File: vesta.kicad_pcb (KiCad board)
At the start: 4 copper layers, 0 parts

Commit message: feat: adding the components to the PCB
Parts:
- added BATTERY1: WAFER-PH2_0-2PWZ, JLCImport:WAFER-PH2_0-2PWZ, F.Cu at (89.5, 66.8)
- added C1: 10uF, Capacitor_SMD:C_0805_2012Metric, F.Cu at (87.2, 84.9)
- added C10: 100nF, PCM_JLCPCB:C_0603, F.Cu at (91.4, 76.1)
- added C11: 100nF, PCM_JLCPCB:C_0603, F.Cu at (91.4, 78.3)
- added C12: 100nF, PCM_JLCPCB:C_0603, F.Cu at (91.4, 80.6)
- added C13: 100nF, PCM_JLCPCB:C_0603, F.Cu at (95.2, 69.3)
- added C14: 4.7uF, PCM_JLCPCB:C_0805, F.Cu at (87.2, 81.9)
- added C15: 100nF, PCM_JLCPCB:C_0603, F.Cu at (95.2, 71.6)
- added C16: 100pF, PCM_JLCPCB:C_0402, F.Cu at (98.6, 80.4)
- added C17: 100pF, PCM_JLCPCB:C_0402, F.Cu at (98.6, 82.2)
- added C18: 100pF, PCM_JLCPCB:C_0402, F.Cu at (98.6, 84.1)
- added C19: 100nF, PCM_JLCPCB:C_0603, F.Cu at (95.2, 73.8)
- added C2: 100nF, Capacitor_SMD:C_0603_1608Metric, F.Cu at (102.0, 85.7)
- added C20: DNP, Capacitor_SMD:C_0603_1608Metric, F.Cu at (102.0, 88.2)
- added C21: DNP, Capacitor_SMD:C_0603_1608Metric, F.Cu at (102.0, 90.8)
- added C22: 100nF, PCM_JLCPCB:C_0603, F.Cu at (95.2, 76.1)
- added C23: 100nF, PCM_JLCPCB:C_0603, F.Cu at (95.2, 78.3)
- added C3: 10uF, PCM_JLCPCB:C_0805, F.Cu at (87.2, 69.7)
- added C4: 10uF, PCM_JLCPCB:C_0805, F.Cu at (87.2, 72.8)
- added C5: 10uF, PCM_JLCPCB:C_0805, F.Cu at (87.2, 75.8)
- added C6: 22uF, PCM_JLCPCB:C_0805, F.Cu at (87.2, 78.9)
- added C7: 470nF, PCM_JLCPCB:C_0603, F.Cu at (91.4, 69.3)
- added C8: 1uF, PCM_JLCPCB:C_0603, F.Cu at (91.4, 71.6)
- added C9: 10nF, PCM_JLCPCB:C_0603, F.Cu at (91.4, 73.8)
- added D1: D_TVS, Diode_SMD:D_SOD-123, F.Cu at (111.0, 87.3)
- added FL1: BALFHB-WL-05D3, JLCImport:BALFHB-WL-05D3, F.Cu at (105.9, 90.2)
- added J1: Solar Panel, JLCImport:WAFER-PH2_0-2PWZ, F.Cu at (95.9, 66.9)
- added J2: Solar Panel, JLCImport:WAFER-PH2_0-2PWZ, F.Cu at (103.1, 66.9)
- added J3: Conn_ARM_SWD_TagConnect_TC2030-NL, Connector:Tag-Connect_TC2030-IDC-NL_2x03_P1.27mm_Vertical, F.Cu at (104.0, 82.0)
- added J4: U.FL, PCM_JLCPCB:IPEX-SMD_BWIPX-1-001E, F.Cu at (113.8, 62.5)
- added JP_TMR_DISABLE1: SolderJumper_2_Open, Jumper:SolderJumper-2_P1.3mm_Open_RoundedPad1.0x1.5mm, F.Cu at (87.2, 88.2)
- added J_EXP1: Conn_01x10, Connector_PinHeader_1.00mm:PinHeader_1x10_P1.00mm_Horizontal, F.Cu at (91.0, 83.2)
- added L1: FTC252012S2R2MBCA, JLCImport:FTC252012S2R2MBCA, F.Cu at (115.7, 87.2)
- added L3: FNR5040S150MT, JLCImport:FNR5040S150MT, F.Cu at (111.6, 82.5)
- added R1: 8.0kΩ, PCM_JLCPCB:R_0603, F.Cu at (99.0, 69.3)
- added R10: 36.5kΩ, PCM_JLCPCB:R_0603, F.Cu at (102.6, 78.3)
- added R11: 100kΩ, PCM_JLCPCB:R_0402, F.Cu at (98.6, 85.9)
- added R12: 100kΩ, PCM_JLCPCB:R_0603, F.Cu at (106.3, 69.3)
- added R13: 0Ω, PCM_JLCPCB:R_0402, F.Cu at (98.6, 87.8)
- added R14: 0kΩ, PCM_JLCPCB:R_0603, F.Cu at (106.3, 71.6)
- added R15: 10kΩ, PCM_JLCPCB:R_0603, F.Cu at (106.3, 73.8)
- added R16: 10kΩ, PCM_JLCPCB:R_0603, F.Cu at (106.3, 76.1)
- added R2: 8.87(or 8.9)kΩ, PCM_JLCPCB:R_0603, F.Cu at (99.0, 71.6)
- added R3: 10kΩ, PCM_JLCPCB:R_0603, F.Cu at (99.0, 73.8)
- added R4: 100kΩ, PCM_JLCPCB:R_0603, F.Cu at (99.0, 76.1)
- added R5: 100kΩ, PCM_JLCPCB:R_0603, F.Cu at (99.0, 78.3)
- added R6: 100kΩ, PCM_JLCPCB:R_0603, F.Cu at (102.6, 69.3)
- added R7: 72kΩ, PCM_JLCPCB:R_0603, F.Cu at (102.6, 71.6)
- added R8: 16.2kΩ, PCM_JLCPCB:R_0603, F.Cu at (102.6, 73.8)
- added R9: 0kΩ, PCM_JLCPCB:R_0603, F.Cu at (102.6, 76.1)
- added TP1: TP_SYS_RAW, TestPoint:TestPoint_Pad_D1.5mm, F.Cu at (115.5, 90.8)
- added TP2: TP_3V3_SYS, TestPoint:TestPoint_Pad_D1.0mm, F.Cu at (116.7, 81.0)
- added TP3: TP_BOOT0, TestPoint:TestPoint_Pad_D1.0mm, F.Cu at (116.7, 84.0)
- added U1: STM32WL55CCU6, JLCImport:STM32WL55CCU6, F.Cu at (112.6, 72.7)
- added U2: BQ24074RGTR, Package_DFN_QFN:MPS_QFN-16_3x3mm_P0.5mm, F.Cu at (111.1, 91.6)
- added U3: TPS63900DSKR, JLCImport:TPS63900DSKR, F.Cu at (109.2, 66.2)
- added U4: BME688_C3664478, JLCImport:BME688_C3664478, F.Cu at (109.1, 62.2)
- added U6: PE4259-63, JLCImport:PE4259-63, F.Cu at (106.1, 86.2)
- added X1: Q13FC1350000400, PCM_JLCPCB:FC-135R_L3.2-W1.5, F.Cu at (114.3, 66.5)
- added X2: X201632MMB4SI, JLCImport:X201632MMB4SI, F.Cu at (87.2, 91.7)

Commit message: feat: making the pinecone
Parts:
- J3: value Conn_ARM_SWD_TagConnect_TC2030-NL -> TagConnect
- moved C21 87.9 mm to (29.5, 41.0), turned to 180 degrees
- moved L1 87.8 mm to (34.2, 54.7), turned to 180 degrees
- moved U6 87.6 mm to (28.1, 46.4)
- moved FL1 85.8 mm to (32.1, 46.4), turned to 180 degrees
- moved C20 85.7 mm to (29.5, 42.5), turned to 180 degrees
- moved TP3 85.6 mm to (48.2, 32.5), turned to 90 degrees
- moved J4 85.1 mm to (39.5, 21.0)
- moved X1 82.1 mm to (40.2, 31.0), turned to 180 degrees
- moved U1 81.6 mm to (39.0, 37.5), turned to 90 degrees
- moved R13 80.5 mm to (32.0, 42.5), turned to 180 degrees
- moved C18 79.4 mm to (30.0, 44.0), turned to 180 degrees
- moved X2 79.3 mm to (36.2, 31.0), turned to 90 degrees
- moved R12 78.2 mm to (32.5, 43.5)
- moved U2 78.0 mm to (40.0, 59.5)
- moved C17 77.5 mm to (30.1, 45.9), turned to -90 degrees
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- renumbered JP_TMR_DISABLE1 to JP_TMR
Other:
- board outline added: 43 x 61.1 mm
- board text added: "()()() ()()()()() ()()()()()() ()()()()()()() ()()()()()()()() ()()()()()()()()() ()()()()()()()()()() ()()()()()()()()()()() ()()()()()()()()()()()() ()()()()()()()()()()() ()()()()()()()()()() ()()()()()()()() ()()()()()"
- board text added: "()()() ()()()()() ()()()()()()() ()()()()()()()() ()()()()()()()()()()() ()()()()()()()()()()() ()()()()()()()()()()()() ()()()()()()()()()()()()() ()()()()()()()()()()()()()() ()()()()()()()()()()()()()()() ()()()()()()()()()()()()()()()() ()()()()()()()()()()()()()()()()() ()()()()()()()()()()()()()()()()() ()()()()()()()()()()()()()()()()() ()()()()()()()()()()()()()()()()() ()()()()()()()()()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"

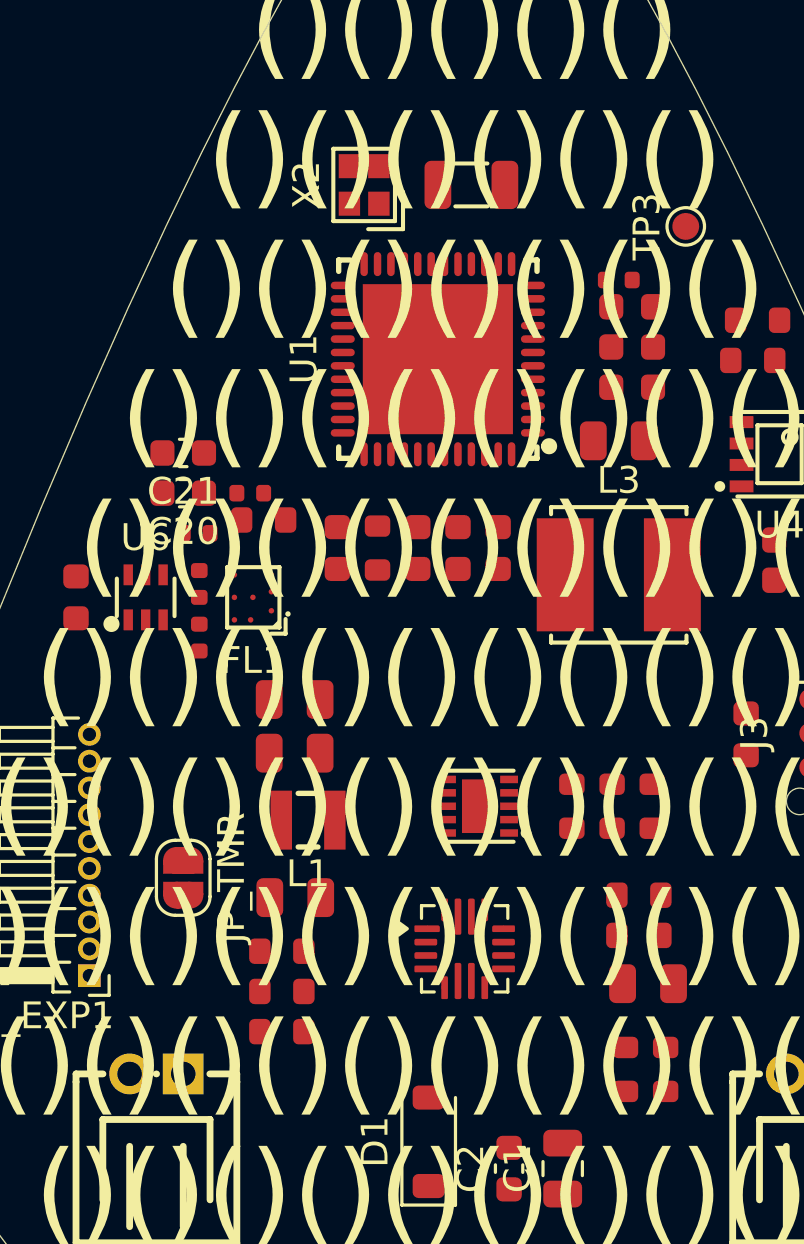
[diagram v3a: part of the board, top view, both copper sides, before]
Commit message: feat: updating the pins in the stm32 footprint
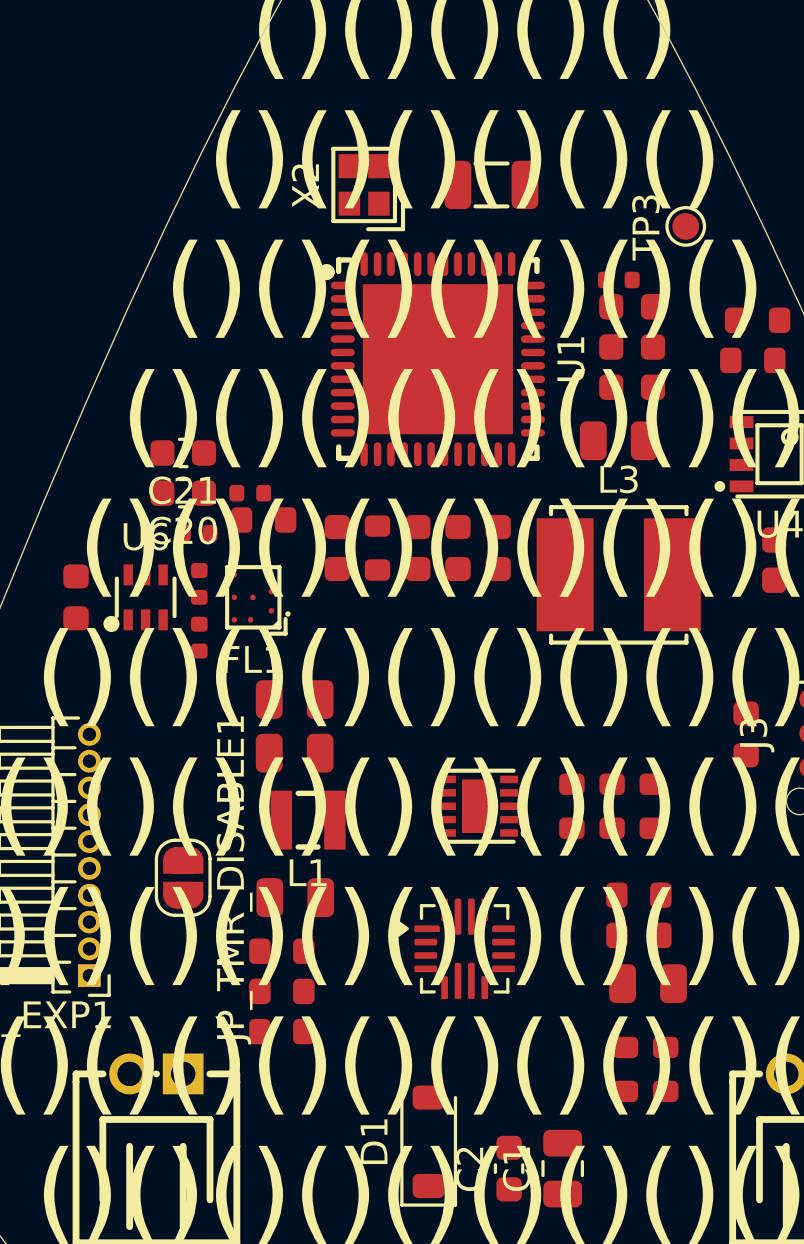
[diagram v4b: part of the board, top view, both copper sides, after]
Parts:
- J3: value TagConnect -> Conn_ARM_SWD_TagConnect_TC2030-NL
- moved X1 0.75 mm to (41.0, 31.0)
- turned U1 to -90 degrees
- renumbered JP_TMR to JP_TMR_DISABLE1
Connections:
- L3 pad 1: unconnected-(L3-Pad1) -> Net-(U1-VLXSMPS)
- U1 pad 1: unconnected-(U1-PB3-Pad1) -> /SWO
- U1 pad 24: unconnected-(U1-VR_PA-Pad24) -> /VR_PA_RF
- U1 pad 25: unconnected-(U1-VDDPA-Pad25) -> /SMPS_1V55
- U1 pad 26: unconnected-(U1-OSC_IN-Pad26) -> /OSC_IN
- U1 pad 47: unconnected-(U1-VLXSMPS-Pad47) -> Net-(U1-VLXSMPS)
- U1 pad 48: unconnected-(U1-VSSSMPS-Pad48) -> GND

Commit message: feat: created the nets
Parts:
- moved U6 25.5 mm to (43.1, 25.8), turned to 180 degrees
- moved C18 19.0 mm to (35.6, 25.8)
- moved C20 18.9 mm to (39.4, 26.3)
- moved C21 18.9 mm to (39.4, 24.8)
- moved R13 18.0 mm to (35.6, 24.8), turned to 0 degrees
- moved X1 10.1 mm to (31.5, 34.5)
- moved X2 9.38 mm to (30.0, 38.0)
- moved J3 2.67 mm to (55.9, 52.7)
- moved J1 1.00 mm to (27.5, 64.2)
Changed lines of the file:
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@@
 	(layers
 		(0 "F.Cu" signal "Front")
-		(4 "In1.Cu" signal)
-		(6 "In2.Cu" signal)
+		(4 "In1.Cu" signal "GND")
+		(6 "In2.Cu" signal "PWR")
 		(2 "B.Cu" signal "Back")
 		(13 "F.Paste" user)
@@
 		(capping no)
 		(filling no)
+		(zone_defaults)
 		(pcbplotparams
 			(layerselection 0x00000000_00000000_55555555_5755f5ff)
@@
 	(footprint "JLCImport:PE4259-63"
 		(layer "F.Cu")
-		(at 28.099314 46.3873)
+		(at 43.149987 25.83998 180)
 		(descr "-40℃~+85℃ 0.35dB 1.8V~3.3V 10MHz~3GHz 30dB 33.5dBm Integrated control logic SPDT SC-70-6 RF Switches ROHS")
 		(tags "C470892 PE4259-63 SC-70-6_L2.2-W1.3-P0.65-LS2.1-BL pSemi")
@@
 		)
 		(property "Manufacturer" "pSemi"
-			(at 0 0 0)
+			(at 0 0 180)
 			(unlocked yes)
 			(layer "F.Fab")
@@
 		)
 		(property "Manufacturer Part" "PE4259-63"
-			(at 0 0 0)
+			(at 0 0 180)
 			(unlocked yes)
 			(layer "F.Fab")
@@
 		(duplicate_pad_numbers_are_jumpers no)
 		(fp_line
-			(start -1.0762 0.701194)
-			(end -1.0762 -0.701194)
+			(start 1.0762 0.701194)
+			(end 1.0762 -0.701194)
 			(stroke
 				(width 0.1524)
@@
 		)
 		(fp_line
-			(start 1.0762 0.701194)
-			(end 1.0762 -0.701194)
+			(start -1.0762 0.701194)
+			(end -1.0762 -0.701194)
 			(stroke
 				(width 0.1524)
@@
 		)
 		(pad "1" smd rect
-			(at -0.649987 0.83998)
+			(at -0.649987 0.83998 180)
 			(size 0.350013 0.78001)
 			(layers "F.Cu" "F.Mask" "F.Paste")
@@
 		)
 		(pad "2" smd rect
-			(at 0 0.83998)
+			(at 0 0.83998 180)
 			(size 0.350013 0.78001)
 			(layers "F.Cu" "F.Mask" "F.Paste")
@@
 		)
 		(pad "3" smd rect
-			(at 0.649987 0.83998)
+			(at 0.649987 0.83998 180)
 			(size 0.350013 0.78001)
 			(layers "F.Cu" "F.Mask" "F.Paste")
@@
 		)
 		(pad "4" smd rect
-			(at 0.649987 -0.83998)
+			(at 0.649987 -0.83998 180)
 			(size 0.350013 0.78001)
 			(layers "F.Cu" "F.Mask" "F.Paste")
@@
 		)
 		(pad "5" smd rect
-			(at 0 -0.83998)
+			(at 0 -0.83998 180)
 			(size 0.350013 0.78001)
 			(layers "F.Cu" "F.Mask" "F.Paste")
@@
 		)
 		(pad "6" smd rect
-			(at -0.649987 -0.83998)
+			(at -0.649987 -0.83998 180)
 			(size 0.350013 0.78001)
 			(layers "F.Cu" "F.Mask" "F.Paste")
@@
 	(footprint "Capacitor_SMD:C_0603_1608Metric"
 		(layer "F.Cu")
-		(at 29.5 42.5 180)
+		(at 39.374987 26.33998 180)
 		(descr "Capacitor SMD 0603 (1608 Metric), square (rectangular) end terminal, IPC-7351 nominal, (Body size source: IPC-SM-782 page 76, https://www.pcb-3d.com/wordpress/wp-content/uploads/ipc-sm-782a_amendment_1_and_2.pdf)")
 		(tags "capacitor")
@@
 	(footprint "JLCImport:X201632MMB4SI"
 		(layer "F.Cu")
-		(at 36.25 31 90)
+		(at 30 38 90)
 		(descr "-40℃~+85℃ 10pF 32MHz Crystal Oscillator ±10ppm ±20ppm SMD2016-4P Crystals ROHS")
 		(tags "C383840 CRYSTAL-SMD_4P-L2.0-W1.6-BL X201632MMB4SI YXC Crystal Oscillators")
@@
 	(footprint "PCM_JLCPCB:C_0402"
 		(layer "F.Cu")
-		(at 30 44 180)
+		(at 35.649987 25.83998 180)
 		(descr "Capacitor SMD 0402 (1005 Metric), square (rectangular) end terminal, IPC_7351 nominal, (Body size source: IPC-SM-782 page 76, https://www.pcb-3d.com/wordpress/wp-content/uploads/ipc-sm-782a_amendment_1_and_2.pdf), generated with kicad-footprint-generator")
 		(tags "capacitor")
@@
 	(footprint "PCM_JLCPCB:R_0402"
 		(layer "F.Cu")
-		(at 32 42.5 180)
+		(at 35.649987 24.83998)
 		(descr "Resistor SMD 0402 (1005 Metric), square (rectangular) end terminal, IPC_7351 nominal, (Body size source: IPC-SM-782 page 72, https://www.pcb-3d.com/wordpress/wp-content/uploads/ipc-sm-782a_amendment_1_and_2.pdf), generated with kicad-footprint-generator")
 		(tags "resistor")
@@
 					(thickness 0.15)
 				)
-				(justify right)
+				(justify left)
 			)
 		)
@@
 		)
 		(property "Datasheet" ""
-			(at 0 0 180)
+			(at 0 0 0)
 			(unlocked yes)
 			(layer "F.Fab")
@@
 		)
 		(property "Description" "Resistor"
-			(at 0 0 180)
+			(at 0 0 0)
 			(unlocked yes)
 			(layer "F.Fab")
@@
 		(duplicate_pad_numbers_are_jumpers no)
 		(fp_line
-			(start 0.9 0.4)
+			(start -0.9 -0.4)
 			(end -0.9 0.4)
 			(stroke
@@
 		)
 		(fp_line
-			(start 0.9 -0.4)
-			(end 0.9 0.4)
+			(start -0.9 -0.4)
+			(end 0.9 -0.4)
 			(stroke
 				(width 0.05)
@@
 		)
 		(fp_line
-			(start -0.9 -0.4)
-			(end 0.9 -0.4)
+			(start 0.9 -0.4)
+			(end 0.9 0.4)
 			(stroke
 				(width 0.05)
@@
 		)
 		(fp_line
-			(start -0.9 -0.4)
+			(start 0.9 0.4)
 			(end -0.9 0.4)
 			(stroke
@@
 		)
 		(pad "1" smd roundrect
-			(at -0.5 0 180)
+			(at -0.5 0)
 			(size 0.56 0.62)
 			(layers "F.Cu" "F.Mask" "F.Paste")
@@
 		)
 		(pad "2" smd roundrect
-			(at 0.5 0 180)
+			(at 0.5 0)
 			(size 0.56 0.62)
 			(layers "F.Cu" "F.Mask" "F.Paste")
@@
 	(footprint "Capacitor_SMD:C_0603_1608Metric"
 		(layer "F.Cu")
-		(at 29.5 41 180)
+		(at 39.374987 24.83998 180)
 		(descr "Capacitor SMD 0603 (1608 Metric), square (rectangular) end terminal, IPC-7351 nominal, (Body size source: IPC-SM-782 page 76, https://www.pcb-3d.com/wordpress/wp-content/uploads/ipc-sm-782a_amendment_1_and_2.pdf)")
 		(tags "capacitor")
@@
 	(footprint "PCM_JLCPCB:FC-135R_L3.2-W1.5"
 		(layer "F.Cu")
-		(at 41 31 180)
+		(at 31.5 34.5 180)
 		(descr "FC-135R_L3.2-W1.5 footprint")
 		(tags "FC-135R_L3.2-W1.5 footprint C32346")
@@
 	(footprint "Connector:Tag-Connect_TC2030-IDC-NL_2x03_P1.27mm_Vertical"
 		(layer "F.Cu")
-		(at 53.516 51.46 -90)
+		(at 55.865 52.73 -90)
 		(descr "Tag-Connect programming header; http://www.tag-connect.com/Materials/TC2030-IDC-NL.pdf")
 		(tags "tag connect programming header pogo pins")
@@
 			(polygon
 				(pts
-					(xy 54.151 52.73) (xy 54.151 50.19) (xy 52.881 50.19) (xy 52.881 52.73)
+					(xy 56.5 54) (xy 56.5 51.46) (xy 55.23 51.46) (xy 55.23 54)
 				)
 			)
@@
 	(footprint "JLCImport:WAFER-PH2_0-2PWZ"
 		(layer "F.Cu")
-		(at 28.499238 64.167526 180)
+		(at 27.5 64.167526 180)
 		(descr "-25℃~+85℃ 1 1x2P 2 250V 2A 2P 2mm 4.7mm 6.05mm 6mm Brass PA66 PH Right Angle Tin UL94V-0 White 弯插,P=2mm Wire To Board Connector ROHS")
 		(tags "C5359610 CONN-TH_2P-P2.00_GP01-2001WR-2P WAFER-PH2.0-2PWZ XUNPU")
@@
 		)
 	)
+	(segment
+		(start 43.149987 24.58998)
+		(end 43.149987 25)
+		(width 0.4)
+		(layer "F.Cu")
+		(net "GND")
+	)
 	(embedded_fonts no)

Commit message: feat: doing all the critical connections
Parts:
- removed R7: 72kΩ, PCM_JLCPCB:R_0603
- moved C19 24.7 mm to (43.5, 29.5), turned to 180 degrees
- moved C16 22.3 mm to (44.0, 30.5), turned to 0 degrees
- moved C17 20.0 mm to (44.0, 31.5), turned to 0 degrees
- moved R12 19.0 mm to (43.5, 28.0), turned to 180 degrees
- moved FL1 16.1 mm to (37.7, 31.3), turned to 90 degrees
- moved C13 15.8 mm to (30.5, 36.5), turned to 180 degrees
- moved BATTERY1 15.4 mm to (54.0, 64.2)
- moved J2 14.2 mm to (40.5, 71.0)
- moved R2 14.2 mm to (46.5, 64.5), turned to 180 degrees
- moved R4 13.9 mm to (46.5, 58.5), turned to 180 degrees
- moved R6 13.7 mm to (35.7, 57.0), turned to 0 degrees
- moved JP_TMR_DISABLE1 13.7 mm to (41.0, 64.3)
- moved C5 13.5 mm to (46.5, 56.5), turned to 180 degrees
- moved R3 13.5 mm to (46.5, 63.0), turned to 180 degrees
- moved C3 13.1 mm to (46.5, 60.5), turned to 0 degrees
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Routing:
- net /3V3_SYS: track 0.00 -> 61.8 mm, vias 0 -> 5
- net GND: track 0.41 -> 36.9 mm
- net /SWCLK: track 0.00 -> 30.1 mm, vias 0 -> 2
- net /SMPS_1V55: track 0.00 -> 30.0 mm
- net /VIN_SOLAR: track 0.00 -> 28.1 mm
- net /RF_SW_CTRL: track 0.00 -> 25.5 mm, vias 0 -> 2
- net /SYS_RAW: track 0.00 -> 20.6 mm
- net /BAT_RAW: track 0.00 -> 16.1 mm
- net /PH3-BOOT0: track 0.00 -> 9.70 mm
- net Net-(U6-RFC): track 0.00 -> 9.20 mm
- net /PC15-OSC32_OUT: track 0.00 -> 8.99 mm
- net Net-(U6-RF2): track 0.00 -> 8.99 mm
- net Net-(J4-In): track 0.00 -> 8.82 mm
- net Net-(U1-VLXSMPS): track 0.00 -> 8.61 mm
- net /VDDA: track 0.00 -> 7.99 mm
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- added copper zone on In2.Cu, net /3V3_SYS
- added copper zone on In1.Cu, net GND

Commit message: feat: finishing all the connections
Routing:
- net /I2C1_SDA: track 6.00 -> 45.2 mm, vias 0 -> 1
- net /I2C1_SCL: track 2.81 -> 37.7 mm, vias 0 -> 1
- net /SWDIO: track 3.84 -> 38.0 mm
- net /EXP_SPI_CS0: track 0.00 -> 32.5 mm, vias 0 -> 1
- net /SPI1_SCK: track 0.00 -> 31.0 mm, vias 0 -> 1
- net /SPI1_MISO: track 0.00 -> 29.9 mm, vias 0 -> 1
- net /EXP_GPIO_CS1: track 0.00 -> 25.6 mm, vias 0 -> 1
- net /EXP_INT_WAKE: track 0.00 -> 24.7 mm, vias 0 -> 1
- net GND: track 36.9 -> 60.3 mm, vias 0 -> 19
- net /SMPS_1V55: track 30.0 -> 49.3 mm
- net Net-(U6-RFC): track 9.20 -> 22.8 mm
- net /3V3_SYS: track 61.8 -> 73.8 mm, vias 5 -> 8
- net /SWO: track 6.80 -> 16.3 mm
- net /SYS_RAW: track 20.6 -> 29.9 mm
- net /RFO_OUT: track 7.19 -> 11.9 mm
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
